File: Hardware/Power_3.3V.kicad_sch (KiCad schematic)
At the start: 11 parts, among them U5 PTPSM863253RDXR

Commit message: Zmieniono złącza, zmieniono kondensatory na kondensatory bezpieczeństwa, poprawiono masę oraz dodano podział na hardware i software
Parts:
- U5: footprint footrpint:RDX0007A-MFG -> footrpint:RDX0007A-MFG_NOVIA
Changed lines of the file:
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@@
 			)
 		)
-		(property "Footprint" "footrpint:RDX0007A-MFG"
+		(property "Footprint" "footrpint:RDX0007A-MFG_NOVIA"
 			(at 157.48 76.2 0)
 			(effects

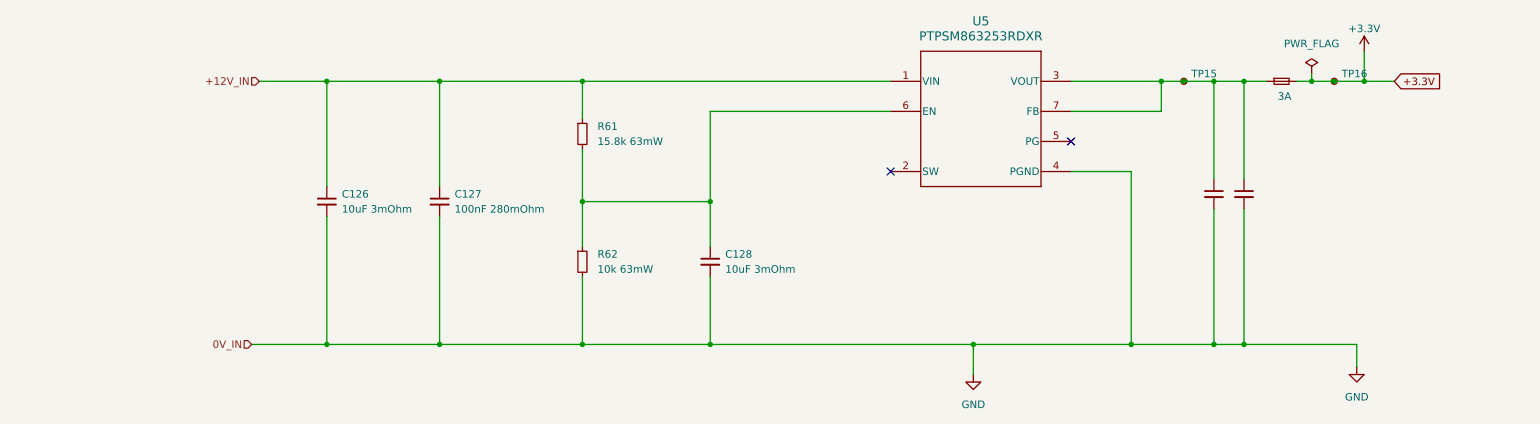
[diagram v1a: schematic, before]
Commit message: Dodano diody TVS na każdej części zasilania, zmieniono bezpieczniki, podzielono bezpieczniki na bezpieczniki do prądów wewnętrznych oraz zewnętrznych,poprawiono małe błedy
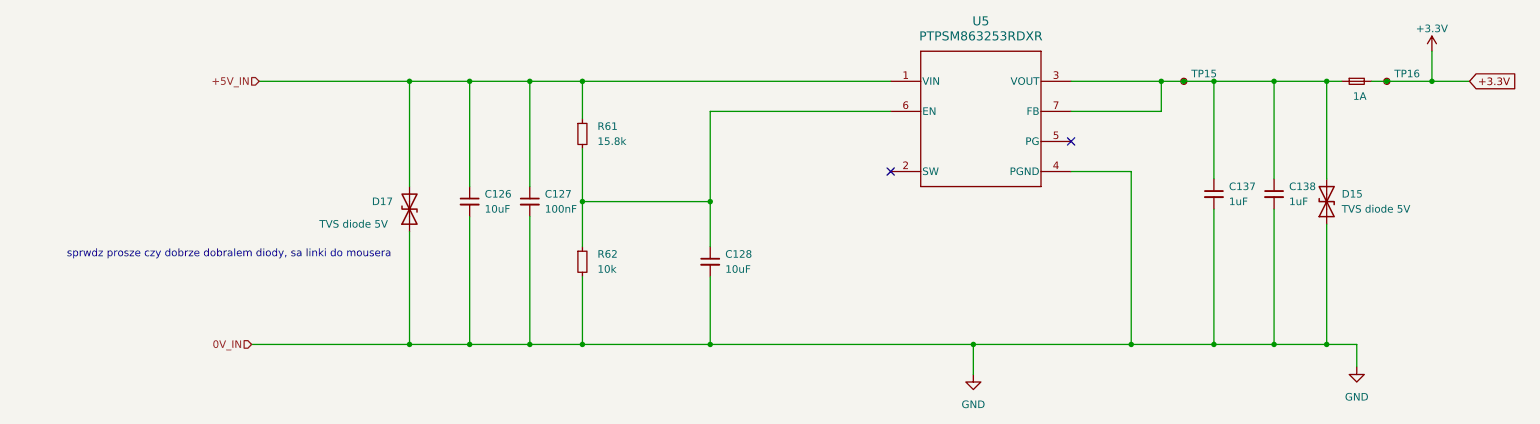
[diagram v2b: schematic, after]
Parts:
- removed F2: 3A, Fuse:Fuse_0603_1608Metric_Pad1.05x0.95mm_HandSolder, symbol Device:Fuse_Small
- added D15: TVS diode 5V, Diode_SMD:D_SOD-882, symbol Device:D_TVS
- added D17: TVS diode 5V, Diode_SMD:D_SOD-323_HandSoldering, symbol Device:D_TVS
- added F5: 1A, Fuse:Fuse_0603_1608Metric_Pad1.05x0.95mm_HandSolder, symbol Device:Fuse_Small
- C126, C128: value 10uF 3mOhm -> 10uF; Field5 (none) -> 10uF 3mOhm
- C127: value 100nF 280mOhm -> 100nF; Field5 (none) -> 100nF 280mOhm
- R61: value 15.8k 63mW -> 15.8k; Field5 (none) -> 15.8k 63mW
- R62: value 10k 63mW -> 10k; Field5 (none) -> 10k 63mW
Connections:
- net +3.3V: now also F5.2
- net GND: now also D15.1 (A1), D17.1 (A1)
- net at C137.1, C138.1, TP15.1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: now also D15.2 (A2), F5.1
- net +12V_IN renamed +5V_IN
- net +5V_IN: now also D17.2 (A2)
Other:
- note added: "sprwdz prosze czy dobrze dobralem diody, sa linki do mousera"
- moved on the sheet: C126, C127, TP16

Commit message: to samo
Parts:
- D15: value TVS diode 5V -> TVS diode 3.3V
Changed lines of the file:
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@@
 			)
 		)
-		(property "Datasheet" "PTPSM863253RDXR"
+		(property "Datasheet" "https://www.mouser.fi/ProductDetail/Texas-Instruments/TPSM863253RDXR?qs=dbcCsuKDzFVdFTfaJMWCkQ%3D%3D"
 			(at 157.48 76.2 0)
 			(effects
@@
 			)
 		)
-		(property "Value" "TVS diode 5V"
+		(property "Value" "TVS diode 3.3V"
 			(at 233.68 97.7899 90)
 			(effects

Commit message: Wersja V1.0 gotowa, wysłana do produckji
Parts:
- removed D15: TVS diode 3.3V, Diode_SMD:D_SOD-882, symbol Device:D_TVS
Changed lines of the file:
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@@
-	)
-	(junction
-		(at 231.14 120.65)
-		(diameter 0)
-		(color 0 0 0 0)
 	)
 	(junction
@@
 	(junction
 		(at 86.36 120.65)
-		(diameter 0)
-		(color 0 0 0 0)
-	)
-	(junction
-		(at 231.14 76.2)
 		(diameter 0)
 		(color 0 0 0 0)
@@
 	(wire
 		(pts
-			(xy 231.14 100.33) (xy 231.14 120.65)
-		)
-		(stroke
-			(width 0)
-			(type default)
-		)
-	)
-	(wire
-		(pts
 			(xy 212.09 120.65) (xy 198.12 120.65)
 		)
@@
 	(wire
 		(pts
-			(xy 231.14 76.2) (xy 231.14 92.71)
-		)
-		(stroke
-			(width 0)
-			(type default)
-		)
-	)
-	(wire
-		(pts
 			(xy 238.76 76.2) (xy 241.3 76.2)
 		)
@@
 	(wire
 		(pts
-			(xy 236.22 120.65) (xy 231.14 120.65)
-		)
-		(stroke
-			(width 0)
-			(type default)
-		)
-	)
-	(wire
-		(pts
 			(xy 76.2 76.2) (xy 76.2 93.98)
 		)
@@
 	(wire
 		(pts
-			(xy 231.14 120.65) (xy 222.25 120.65)
+			(xy 222.25 120.65) (xy 236.22 120.65)
 		)
 		(stroke
@@
 	(wire
 		(pts
-			(xy 231.14 76.2) (xy 233.68 76.2)
+			(xy 222.25 76.2) (xy 233.68 76.2)
 		)
 		(stroke
@@
 		(pts
 			(xy 105.41 96.52) (xy 105.41 104.14)
-		)
-		(stroke
-			(width 0)
-			(type default)
-		)
-	)
-	(wire
-		(pts
-			(xy 222.25 76.2) (xy 231.14 76.2)
 		)
 		(stroke
@@
 					(unit 1)
 				)
-			)
-		)
-	)
-	(symbol
-		(lib_id "Device:D_TVS")
-		(at 231.14 96.52 90)
-		(unit 1)
-		(exclude_from_sim no)
-		(in_bom yes)
-		(on_board yes)
-		(dnp no)
-		(fields_autoplaced yes)
-		(property "Reference" "D15"
-			(at 233.68 95.2499 90)
-			(effects
-				(font
-					(size 1.27 1.27)
-				)
-				(justify right)
-			)
-		)
-		(property "Value" "TVS diode 3.3V"
-			(at 233.68 97.7899 90)
-			(effects
-				(font
-					(size 1.27 1.27)
-				)
-				(justify right)
-			)
-		)
-		(property "Footprint" "Diode_SMD:D_SOD-882"
-			(at 231.14 96.52 0)
-			(effects
-				(font
-					(size 1.27 1.27)
-				)
-				(hide yes)
-			)
-		)
-		(property "Datasheet" "https://www.mouser.pl/ProductDetail/Littelfuse/SP3205-01ETG?qs=vHuUswq2%252BswfNhVD4WkB%252BQ%3D%3D"
-			(at 231.14 96.52 0)
-			(effects
-				(font
-					(size 1.27 1.27)
-				)
-				(hide yes)
-			)
-		)
-		(property "Description" "Bidirectional transient-voltage-suppression diode"
-			(at 231.14 96.52 0)
-			(effects
-				(font
-					(size 1.27 1.27)
-				)
-				(hide yes)
-			)
-		)
-		(pin "1"
-		)
-		(pin "2"
-		)
-		(instances
-			(project "BMS"
-				(path "/26289bb6-56bc-4ca1-b1a2-18d58d1afdf5/b306fb08-ef5e-4bf5-8efa-c4e5200f566a/36deb01f-8567-4cbb-9333-b925b4509962"
-					(reference "D15")
-					(unit 1)
-				)

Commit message: zmiany w kodzier bq
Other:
- note removed: "sprwdz prosze czy dobrze dobralem diody, sa linki do mousera"
- moved on the sheet: TP16
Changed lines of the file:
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@@
 	(generator_version "9.0")
 	(paper "A4")
-	(text "sprwdz prosze czy dobrze dobralem diody, sa linki do mousera"
-		(exclude_from_sim no)
-		(at 45.72 105.41 0)
-		(effects
-			(font
-				(size 1.27 1.27)
-			)
-		)
-	)
 	(junction
 		(at 171.45 120.65)
@@
 	)
 	(junction
-		(at 241.3 76.2)
-		(diameter 0)
-		(color 0 0 0 0)
-	)
-	(junction
 		(at 86.36 76.2)
 		(diameter 0)
@@
 	)
 	(junction
-		(at 248.92 76.2)
+		(at 237.49 76.2)
 		(diameter 0)
 		(color 0 0 0 0)
@@
 	)
 	(junction
+		(at 229.87 76.2)
+		(diameter 0)
+		(color 0 0 0 0)
+	)
+	(junction
+		(at 96.52 120.65)
+		(diameter 0)
+		(color 0 0 0 0)
+	)
+	(junction
 		(at 222.25 76.2)
-		(diameter 0)
-		(color 0 0 0 0)
-	)
-	(junction
-		(at 96.52 120.65)
 		(diameter 0)
 		(color 0 0 0 0)
@@
 	(wire
 		(pts
-			(xy 248.92 71.12) (xy 248.92 76.2)
+			(xy 237.49 74.93) (xy 237.49 76.2)
 		)
 		(stroke
@@
 	(wire
 		(pts
+			(xy 228.6 76.2) (xy 229.87 76.2)
+		)
+		(stroke
+			(width 0)
+			(type default)
+		)
+	)
+	(wire
+		(pts
 			(xy 212.09 120.65) (xy 198.12 120.65)
 		)
@@
 	(wire
 		(pts
-			(xy 238.76 76.2) (xy 241.3 76.2)
-		)
-		(stroke
-			(width 0)
-			(type default)
-		)
-	)
-	(wire
-		(pts
 			(xy 105.41 82.55) (xy 105.41 76.2)
 		)
@@
 	(wire
 		(pts
+			(xy 222.25 76.2) (xy 222.25 92.71)
+		)
+		(stroke
+			(width 0)
+			(type default)
+		)
+	)
+	(wire
+		(pts
 			(xy 207.01 76.2) (xy 203.2 76.2)
 		)
@@
 	(wire
 		(pts
-			(xy 222.25 92.71) (xy 222.25 76.2)
-		)
-		(stroke
-			(width 0)
-			(type default)
-		)
-	)
-	(wire
-		(pts
 			(xy 76.2 120.65) (xy 86.36 120.65)
 		)
@@
 	(wire
 		(pts
-			(xy 241.3 76.2) (xy 248.92 76.2)
+			(xy 229.87 76.2) (xy 237.49 76.2)
 		)
 		(stroke
@@
 	(wire
 		(pts
-			(xy 222.25 76.2) (xy 233.68 76.2)
+			(xy 222.25 76.2) (xy 223.52 76.2)
 		)
 		(stroke
@@
 	(wire
 		(pts
-			(xy 248.92 76.2) (xy 255.27 76.2)
+			(xy 237.49 76.2) (xy 243.84 76.2)
 		)
 		(stroke
@@
 	(global_label "+3.3V"
 		(shape input)
-		(at 255.27 76.2 0)
+		(at 243.84 76.2 0)
 		(fields_autoplaced yes)
 		(effects
@@
 		)
 		(property "Intersheetrefs" "${INTERSHEET_REFS}"
-			(at 263.94 76.2 0)
+			(at 252.51 76.2 0)
 			(effects
 				(font
@@
 	(symbol
 		(lib_id "power:+3.3V")
-		(at 248.92 71.12 0)
+		(at 237.49 74.93 0)
 		(unit 1)
 		(exclude_from_sim no)
@@
 		(dnp no)
 		(property "Reference" "#PWR01"
-			(at 248.92 74.93 0)
+			(at 237.49 78.74 0)
 			(effects
 				(font
@@
 		)
 		(property "Value" "+3.3V"
-			(at 248.92 67.31 0)
+			(at 237.49 71.12 0)
 			(effects
 				(font
@@
 		)
 		(property "Footprint" ""
-			(at 248.92 71.12 0)
+			(at 237.49 74.93 0)
 			(effects
 				(font
@@
 		)
 		(property "Datasheet" ""
-			(at 248.92 71.12 0)
+			(at 237.49 74.93 0)
 			(effects
 				(font
@@
 		)
 		(property "Description" ""
-			(at 248.92 71.12 0)
+			(at 237.49 74.93 0)
 			(effects
 				(font
@@
 	(symbol
 		(lib_id "Connector:TestPoint_Small")
-		(at 241.3 76.2 0)
+		(at 229.87 76.2 0)
 		(unit 1)
 		(exclude_from_sim no)
@@
 		(fields_autoplaced yes)
 		(property "Reference" "TP16"
-			(at 242.57 74.9299 0)
+			(at 231.14 74.9299 0)
 			(effects
 				(font
@@
 		)
 		(property "Value" "TestPoint_Small"
-			(at 242.57 77.4699 0)
+			(at 231.14 77.4699 0)
 			(effects
 				(font
@@
 		)
 		(property "Footprint" "TestPoint:TestPoint_Pad_D1.0mm"
-			(at 246.38 76.2 0)
+			(at 234.95 76.2 0)
 			(effects
 				(font
@@
 		)
 		(property "Datasheet" "~"
-			(at 246.38 76.2 0)
+			(at 234.95 76.2 0)
 			(effects
 				(font
@@
 		)
 		(property "Description" "test point"
-			(at 241.3 76.2 0)
+			(at 229.87 76.2 0)
 			(effects
 				(font
@@
 	(symbol
 		(lib_id "Device:Fuse_Small")
-		(at 236.22 76.2 0)
+		(at 226.06 76.2 0)
 		(unit 1)
 		(exclude_from_sim no)
@@
 		(dnp no)
 		(property "Reference" "F5"
-			(at 233.426 74.422 0)
+			(at 223.266 74.422 0)
 			(effects
 				(font
@@
 		)
 		(property "Value" "1A"
-			(at 236.728 78.74 0)
+			(at 226.568 78.74 0)
 			(effects
 				(font
@@
 		)
 		(property "Footprint" "Fuse:Fuse_0603_1608Metric_Pad1.05x0.95mm_HandSolder"
-			(at 236.22 76.2 0)
+			(at 226.06 76.2 0)
 			(effects
 				(font
@@
 		)
 		(property "Datasheet" "https://www.mouser.pl/ProductDetail/Bourns/SF-0603F100-2?qs=sGAEpiMZZMsIz3CjQ1xegdp54%252BzS9Epn%252B5yJC0KdyEI%3D"
-			(at 236.22 76.2 0)
+			(at 226.06 76.2 0)
 			(effects
 				(font
@@
 		)
 		(property "Description" "Fuse, small symbol"
-			(at 236.22 76.2 0)
-			(effects
-				(font
+			(at 226.06 76.2 0)
+			(effects
+				(font
